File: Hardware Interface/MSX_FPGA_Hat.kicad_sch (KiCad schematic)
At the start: 40 parts, among them J1 Conn_01x03_Female, J2 Soundin, J3 AudioJack3, J4 /CS12, Q1 2N3904, Q2 2N3904, SW1 RESET, U1 74LVC245, U2 74LVC245, U3 74LVC245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

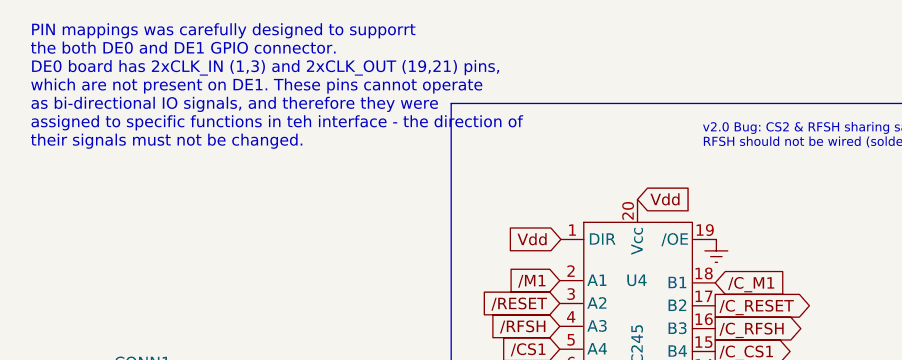
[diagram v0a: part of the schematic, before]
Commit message: fixed typos in the schematic info text
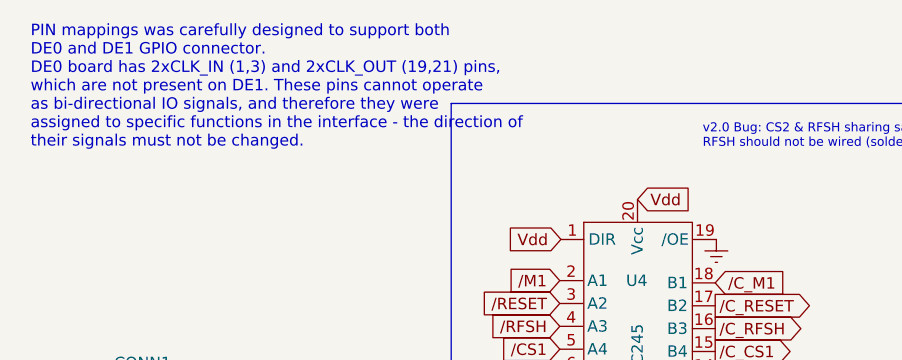
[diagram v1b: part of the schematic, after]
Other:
- note added: "PIN mappings was carefully designed to support both DE0 and DE1 GPIO connector. DE0 board has 2xCLK_IN (1,3) and 2xCLK_OUT (19,21) pins, which are not present on DE1. These pins cannot operate as bi-directional IO signals, and therefore they were assigned to specific functions in the interface - the direction of their signals must not be changed."
- note removed: "PIN mappings was carefully designed to supporrt the both DE0 and DE1 GPIO connector. DE0 board has 2xCLK_IN (1,3) and 2xCLK_OUT (19,21) pins, which are not present on DE1. These pins cannot operate as bi-directional IO signals, and therefore they were assigned to specific functions in teh interface - the direction of their signals must not be changed."
